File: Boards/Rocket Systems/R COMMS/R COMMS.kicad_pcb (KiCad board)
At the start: 4 copper layers, 75 x 40 mm, 87 parts, among them IC1 NSVT30010MXV6T1G, IC2 NSVT30010MXV6T1G, J1 BM03B-SRSS-TBLFSN, J2 22285061, J3 DX07S016JA1R1500, J4 MEM2061-01-188-00-A_REVA, J5 1190297, J6 SMARA_CONNECTOR, U1 W25Q128JVSIQ TR, U2 ESD7L5.0DT5G, U3 SX1280IMLTRT, U4 NRF21540-QDAA-R, U5 ST1L05APU33R, U6 MAX485CSA+T, U7 VLMKG3400-GS08, U8 STLM20DD9F, U9 VLMKG3400-GS08

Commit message: 3D Symbols Update and R Comms PCB layout (1)
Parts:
- D1: value PMEG2010ER -> RSX301L-30DDTE25; footprint Diode-Schottky_PMEG2010ER:SODFL3517X110N -> Diode-Schottky_RSX301L:DIOM5026X220N
- J2: moved to B.Cu
- moved J4 179.4 mm to (168.4, 80.3), turned to 90 degrees
- moved C1 175.5 mm to (158.0, 80.0)
- moved R30 156.0 mm to (142.9, 59.6), turned to -90 degrees
- moved R31 153.1 mm to (144.8, 64.8), turned to -90 degrees
- moved R29 152.8 mm to (144.8, 59.7)
- moved U6 145.3 mm to (149.9, 62.2), turned to 0 degrees
- moved CV4 141.7 mm to (125.2, 75.6), turned to 0 degrees
- moved R28 138.9 mm to (156.8, 60.4)
- moved R26 135.9 mm to (154.9, 62.2), turned to -90 degrees
- moved CV1 135.2 mm to (125.2, 74.3), turned to 180 degrees
- moved R27 134.9 mm to (156.8, 64.2)
- moved CV6 134.8 mm to (137.7, 77.5), turned to 0 degrees
- moved MCU1 130.7 mm to (131.4, 74.9)
- moved CV8 129.7 mm to (130.2, 68.6)
- moved CV3 128.4 mm to (137.7, 76.2), turned to 0 degrees
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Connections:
- net CRYSTAL renamed /RP2040/Crystal
- J3 pad 11: Net-(D1-PadA) -> Net-(D1-A)
- J3 pad 2: Net-(D1-PadA) -> Net-(D1-A)
- J4 pad 9: /SD-Card SPI MISO -> GND
- J5 pad 1: /RS_B -> /RS_A
- J5 pad 2: /RS_B -> /RS_A
- J5 pad 3: /RS_A -> /RS_B
- J5 pad 4: /RS_A -> /RS_B
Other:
- board size 75 x 40 mm -> 75 x 35 mm

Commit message: R COMMS layout placement
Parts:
- C19, C20, C21, C23, C24, C27, C28, C32, C33, C34, C35, CV12, CV14, CV15, CV16, CV17, CV2, CV3, CV4, D1, IC1, IC2, L2, L3, L4, R12, R14, R15, R16, R26, R27, R28, R29, R30, R31, R8, R9, U3, U4, U5, U6, XTAL2: moved to B.Cu
- R2, R3: footprint Resistor-0603:RES_0603 -> Resistor-0402:RES_0402
- moved R6 178.5 mm to (108.3, 81.5)
- moved R5 176.9 mm to (105.9, 76.4)
- moved XTAL1 176.3 mm to (116.1, 70.7), turned to -90 degrees
- moved R4 175.2 mm to (106.6, 79.0), turned to 0 degrees
- moved R1 170.3 mm to (110.4, 80.9), turned to 0 degrees
- moved J1 167.4 mm to (102.7, 78.0), turned to -90 degrees
- moved R7 167.3 mm to (117.2, 67.3)
- moved CV13 151.4 mm to (118.8, 71.2)
- moved CV5 150.9 mm to (120.8, 83.8), turned to -90 degrees
- moved R13 150.8 mm to (141.3, 78.1), turned to 180 degrees
- moved CV9 148.5 mm to (115.8, 78.0), turned to 180 degrees
- moved CV14 147.7 mm to (127.5, 77.6), turned to 0 degrees
- moved CV7 146.2 mm to (125.6, 72.4), turned to 0 degrees
- moved S3 145.9 mm to (110.0, 85.1)
- moved CV12 144.2 mm to (127.5, 78.9), turned to 0 degrees
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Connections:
- U2 pad 1: /RP2040/USB_DM -> unconnected-(U2-Pad1)
- U2 pad 2: /RP2040/USB_DP -> unconnected-(U2-Pad2)
- U2 pad 3: GND -> unconnected-(U2-Pad3)
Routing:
- net Net-(J1-Pad1): track 0.00 -> 1.91 mm
- net Net-(J1-Pad3): track 0.00 -> 1.81 mm
- net /RS_A: track 0.00 -> 0.50 mm

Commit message: 3D models update
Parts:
- CR2, CR3: footprint LED-Yellow_VLMY1300-GS08:LED_VISHAY_VLMX1300_VIS -> LED-Yellow_VLMY1300-GS08:LEDC1608X100N
- XTAL1: footprint AS12MHz:ASE-3.2X2.5_ABR -> AS12MHz:ASE24576MHZLCT
- moved CV13 7.18 mm to (111.6, 71.9), turned to -90 degrees
- moved R7 2.22 mm to (115.0, 67.6), turned to 0 degrees
- moved R26 1.36 mm to (151.4, 65.3)
- moved R27 1.36 mm to (152.7, 63.9)
- moved R29 1.36 mm to (142.4, 67.8)
- moved R31 1.36 mm to (142.4, 62.5)
- moved U6 1.36 mm to (146.9, 65.3)
- moved R30 1.36 mm to (141.1, 62.5)
- moved R28 1.25 mm to (152.7, 66.8)
- moved XTAL1 1.07 mm to (115.0, 70.9)
- moved L1 0.60 mm to (109.0, 69.3), turned to 90 degrees
- moved J5 0.28 mm to (156.5, 67.8)
- moved L4 0.20 mm to (100.8, 81.3)
- moved CR2 0.13 mm to (151.2, 76.6)
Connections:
- J5 pad 1: /RS_A -> /RS_B
- J5 pad 2: /RS_A -> /RS_B
- J5 pad 3: /RS_B -> /RS_A
- J5 pad 4: /RS_B -> /RS_A
- U2 pad 1: unconnected-(U2-Pad1) -> /RP2040/USB_DP
- U2 pad 2: unconnected-(U2-Pad2) -> /RP2040/USB_DM
- U2 pad 3: unconnected-(U2-Pad3) -> GND
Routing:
- net /RS_A: track 0.50 -> 0.00 mm

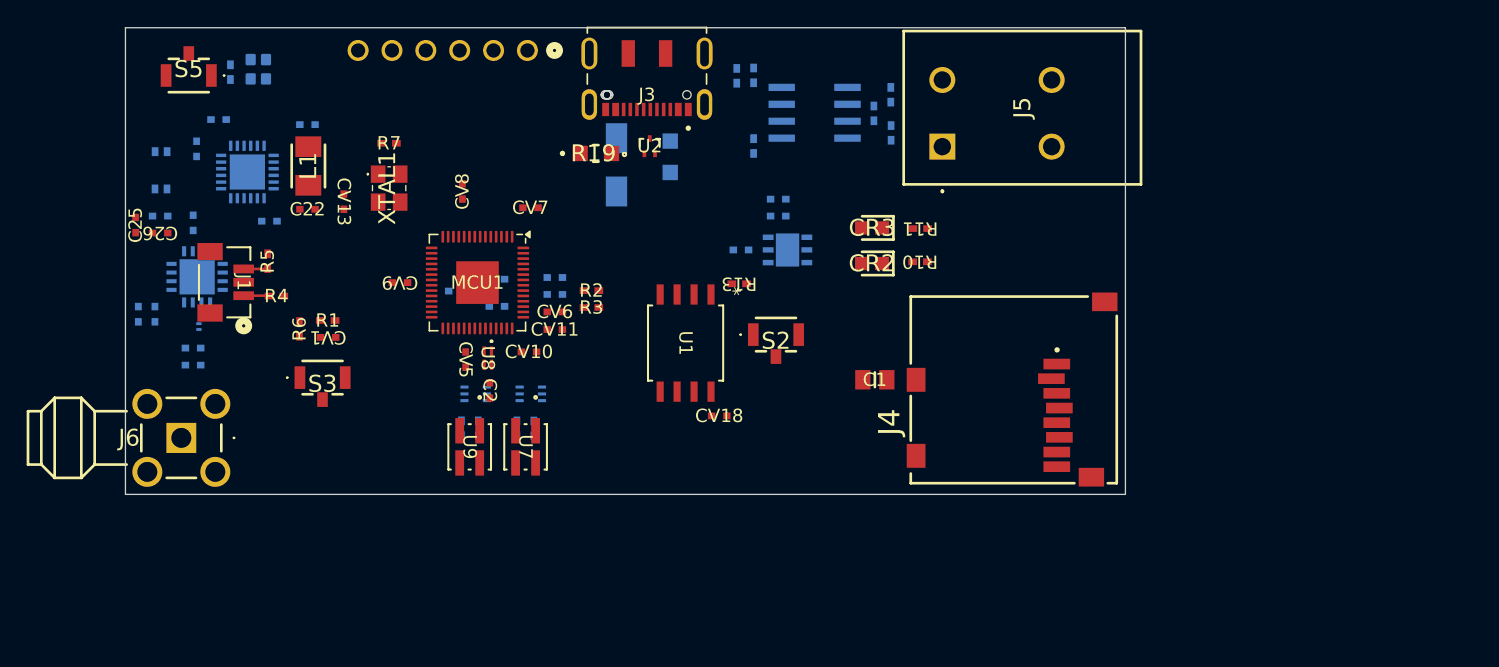
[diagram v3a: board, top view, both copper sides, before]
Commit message: R COMMS layout placement update
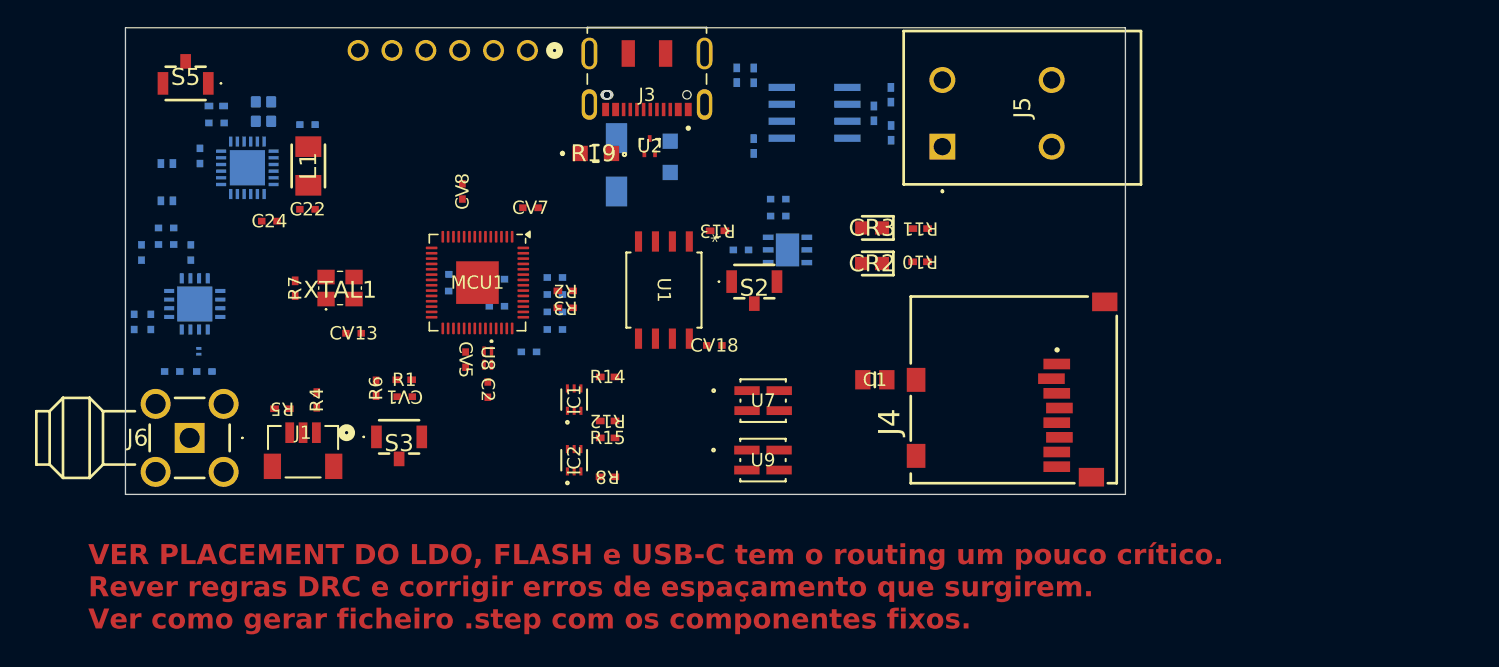
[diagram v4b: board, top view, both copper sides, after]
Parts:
- C24, IC1, IC2, R12, R14, R15, R8: moved to F.Cu
- C25, C26, CV10, CV11, CV6, CV9: moved to B.Cu
- moved U9 22.0 mm to (143.1, 91.3), turned to 0 degrees
- moved U7 18.2 mm to (143.1, 86.9), turned to 0 degrees
- moved J1 14.0 mm to (108.6, 90.7), turned to 0 degrees
- moved R7 12.9 mm to (108.0, 78.4), turned to 90 degrees
- moved R8 11.5 mm to (131.4, 92.6), turned to 180 degrees
- moved R5 11.1 mm to (107.0, 87.5), turned to 180 degrees
- moved CV13 9.90 mm to (112.4, 81.8), turned to 0 degrees
- moved R15 9.72 mm to (131.4, 89.7), turned to 0 degrees
- moved IC2 8.91 mm to (128.9, 91.3), turned to 90 degrees
- moved R4 8.36 mm to (109.6, 86.8), turned to 90 degrees
- moved XTAL1 8.35 mm to (111.3, 78.4), turned to 0 degrees
- moved R6 7.26 mm to (114.0, 85.9)
- moved S3 7.26 mm to (115.8, 89.6)
- moved CV1 7.26 mm to (116.2, 86.6)
- moved R1 7.26 mm to (116.2, 85.3)
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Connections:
- C2 pad 2: Net-(U8-GND) -> GND
- U8 pad 3: Net-(U8-GND) -> GND
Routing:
- net Net-(J1-Pad1): track 1.91 -> 0.00 mm
- net Net-(J1-Pad3): track 1.81 -> 0.00 mm
- added copper zone on In2.Cu, net GND
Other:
- board text added: "VER PLACEMENT DO LDO, FLASH e USB-C tem o routing um pouco crítico. Rever regras DRC e corrigir erros de espaçamento que surgirem. Ver como gerar ficheiro .step com os componentes fixos."

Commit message: full update on RCOMMS layout
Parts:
- removed R12, R14: 100, Resistor-0402:RES_0402
- removed R31: 10K, Resistor-0402:RES_0402
- removed S2, S3, S5: TL1017AABF160QG, E-Switch_Small:TL1017AABF160QG
- added C29: 4.7u, Capacitor-0402:Capacitor_0402, F.Cu at (129.9, 63.4)
- added C30: 100nF, Capacitor-0402:Capacitor_0402, F.Cu at (162.8, 81.9)
- added C31: 100nF, Capacitor-0402:Capacitor_0402, F.Cu at (160.8, 73.7)
- added C36: 100n, Capacitor-0402:Capacitor_0402, F.Cu at (156.5, 72.1)
- added C37: 100nF, Capacitor-0402:Capacitor_0402, F.Cu at (161.6, 81.9)
- added C38: 100nF, Capacitor-0402:Capacitor_0402, F.Cu at (160.8, 75.0)
- added C39: 100nF, Capacitor-0402:Capacitor_0402, F.Cu at (175.8, 65.2)
- added C40: 4.7u, Capacitor-0402:Capacitor_0402, F.Cu at (129.9, 64.6)
- added C41: 100nF, Capacitor-0402:Capacitor_0402, F.Cu at (119.3, 64.8)
- added H1: MountingHole, MountingHole:MountingHole_3.2mm_M3_ISO7380_Pad_TopBottom, F.Cu at (110.0, 63.0)
- added H2: MountingHole, MountingHole:MountingHole_3.2mm_M3_ISO7380_Pad_TopBottom, F.Cu at (170.0, 63.0)
- added H3: MountingHole, MountingHole:MountingHole_3.2mm_M3_ISO7380_Pad_TopBottom, F.Cu at (110.0, 92.0)
- added H4: MountingHole, MountingHole:MountingHole_3.2mm_M3_ISO7380_Pad_TopBottom, F.Cu at (170.0, 92.0)
- added IC3: THVD2412VDR, THVD2412VDR:SOIC127P600X175-14N, F.Cu at (166.8, 76.8)
- added JP1: Jumper_2_Bridged, Jumper:SolderJumper-2_P1.3mm_Open_RoundedPad1.0x1.5mm, B.Cu at (109.2, 82.0)
- added JP2: Jumper_2_Bridged, Jumper:SolderJumper-2_P1.3mm_Open_RoundedPad1.0x1.5mm, B.Cu at (142.2, 92.0)
- added JP3: Jumper_2_Bridged, Jumper:SolderJumper-2_P1.3mm_Open_RoundedPad1.0x1.5mm, B.Cu at (134.4, 67.1)
- added LS1: PKLCS1212E20A0-R1, PKLCS1212E20A0-R1:PKLCS1212E20A0-R1, B.Cu at (151.9, 80.5)
- added MP1: S0991-46R, S0991-46R:S099146R, F.Cu at (93.0, 76.3)
- added MP2: S0991-46R, S0991-46R:S099146R, F.Cu at (118.0, 76.5)
- added MP3: S0991-46R, S0991-46R:S099146R, F.Cu at (103.0, 66.5)
- added MP4: S0991-46R, S0991-46R:S099146R, F.Cu at (111.0, 86.5)
- added R17: 1k, Resistor-0402:RES_0402, F.Cu at (153.1, 76.4)
- added R18: 1k, Resistor-0402:RES_0402, F.Cu at (152.7, 82.3)
- added R21: 10k, Resistor-0402:RES_0402, F.Cu at (164.2, 81.9)
- added R22: 10k, Resistor-0402:RES_0402, F.Cu at (172.7, 74.9)
- added R23: 10k, Resistor-0402:RES_0402, F.Cu at (172.7, 73.7)
- added R24: 120, Resistor-0402:RES_0402, F.Cu at (166.1, 72.3)
- added R25: 120, Resistor-0402:RES_0402, F.Cu at (168.7, 72.3)
- C19, C20, C21, C23, C25, C26, C27, C28, C32, C33, C34, C35, CV10, CV11, CV12, CV14, CV15, CV16, CV17, CV2, CV3, CV4, CV6, CV9, D1, L2, L3, L4, R16, U3, U4, U5, XTAL2: moved to F.Cu
- IC1: value NSVT30010MXV6T1G -> BC846BLT1G; footprint 2 PNP:SOT-563_1P3X1P7_ONS -> BJT NPN:SOT96P237X111-3N
- J5: value 1190297 -> 5023520600; footprint LPT Conn 2 Entradas:1190297 -> 5023520600:CONN06_502352_MOL
- MCU1: footprint Package_DFN_QFN:QFN-56-1EP_7x7mm_P0.4mm_EP3.2x3.2mm -> RP2040:QFN56_7X7_RPI
- R19: footprint Resistor-0805:RES_0805 -> Resistor-0402:RES_0402
- R26: value 120 -> 523; moved to F.Cu
- R27, R28: value 20K -> 523; moved to F.Cu
- R29: value 10K -> 523; moved to F.Cu
- R30: value 10K -> 10k; moved to F.Cu
- R9: footprint Resistor-0805:RES_0805 -> Resistor-0402:RES_0402; moved to F.Cu
- U2: value ESD7L5.0DT5G -> IP4220CZ6; footprint ESD7L5-Diode:SOT-723_0P85X1P25_ONS -> IP4220CZ6:SOT457_NEX
- U6: value MAX485CSA+T -> IP4220CZ6; footprint RS Transceiver:21-0041-3-M_90-0096-8L_MXM -> IP4220CZ6:SOT457_NEX; moved to F.Cu
- U7: value VLMKG3400-GS08 -> IP4220CZ6; footprint VLMKG3400-GS08:SMT_00-GS08_VIS -> IP4220CZ6:SOT457_NEX
- moved R30 32.2 mm to (166.7, 81.9), turned to 90 degrees
- moved R29 31.8 mm to (172.7, 77.3), turned to 0 degrees
- moved U7 30.1 mm to (122.7, 64.8), turned to 180 degrees
- moved U6 29.1 mm to (175.8, 68.6), turned to 90 degrees
- moved J5 28.1 mm to (184.5, 70.6)
- moved R8 28.0 mm to (159.1, 88.1), turned to -90 degrees
- moved IC2 27.7 mm to (156.6, 90.5), turned to 180 degrees
- moved J1 27.5 mm to (136.1, 91.9)
- moved R5 27.5 mm to (134.5, 88.7)
- moved R6 26.7 mm to (140.4, 90.6)
- moved R1 26.5 mm to (142.3, 90.0), turned to 180 degrees
- moved CV1 26.5 mm to (142.3, 91.3), turned to 0 degrees
- moved IC1 25.0 mm to (152.7, 79.0), turned to -90 degrees
- moved R15 22.8 mm to (154.2, 88.1), turned to 90 degrees
- moved R4 22.5 mm to (131.8, 90.6)
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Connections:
- net Net-(MCU1-USB_DM) renamed /RP2040/USB_D-
- net Net-(MCU1-USB_DP) renamed /RP2040/USB_D+
- D1 pad 2: Net-(D1-A) -> VBUS
- IC1 pad 2: /Status2 Green -> GND
- IC1 pad 3: GND -> Net-(IC1-C)
- J2 pad 2: /OBC UART TX -> GND
- J2 pad 3: /OBC UART RX -> /OBC UART TX
- J2 pad 4: /OBC UART CTS -> /OBC UART RX
- J2 pad 5: /OBC UART RTS -> /OBC UART CTS
- J2 pad 6: GND -> /OBC UART RTS
- J3 pad 11: Net-(D1-A) -> VBUS
- J3 pad 2: Net-(D1-A) -> VBUS
- J3 pad 5: /RP2040/USB_DM -> /RP2040/USB_DN
- J3 pad 8: /RP2040/USB_DM -> /RP2040/USB_DN
- J5 pad 1: /RS_B -> /Pyro Main Chute
- J5 pad 2: /RS_B -> /Pyro Drogue
- J5 pad 3: /RS_A -> /RS-TX_DP
- J5 pad 4: /RS_A -> /RS-TX_DN
- MCU1 pad 40: /Status2 Green -> /Pyro Main Chute
- MCU1 pad 41: /Status2 Red -> /Pyro Drogue
- MCU1 pad 6: /RS_RX -> /RS_TX
- MCU1 pad 7: /RS_TX -> /RS_RX
- MCU1 pad 8: /RS_ENABLE -> /Buzzer
- R19 pad 1: GND -> Net-(J3-CC2)
- R19 pad 2: Net-(J3-CC2) -> GND
- R26 pad 1: /RS_B -> /RS-RX_DN
- R26 pad 2: /RS_A -> GND
- R27 pad 2: /RS_A -> /RS-RX_DP
- R28 pad 1: /RS_B -> +5V
- R28 pad 2: GND -> /RS-TX_DP
- R29 pad 1: +3.3V -> /RS-TX_DN
- R29 pad 2: /RS_RX -> GND
- R3 pad 1: /RP2040/USB_DM -> /RP2040/USB_DN
- R30 pad 2: /RS_ENABLE -> Net-(IC3-DE)
- U2 pad 2: /RP2040/USB_DM -> GND
- U2 pad 3: GND -> /RP2040/USB_DN
- U6 pad 1: /RS_RX -> /RS-TX_DN
- U6 pad 2: /RS_ENABLE -> GND
- U6 pad 3: /RS_ENABLE -> /RS-TX_DP
- U6 pad 4: /RS_TX -> /RS-RX_DN
- U6 pad 5: GND -> +5V
- U6 pad 6: /RS_A -> /RS-RX_DP
- U7 pad 1: +5V -> /OBC UART TX
- U7 pad 2: Net-(U7-A_Green) -> GND
- U7 pad 3: +5V -> /OBC UART RX
- U7 pad 4: Net-(U7-A_Red) -> /OBC UART RTS
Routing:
- net /OBC UART CTS: track 0.00 -> 19.9 mm
- net /OBC UART TX: track 0.00 -> 18.8 mm
- net /RP2040/USB_DN: track 0.00 -> 18.2 mm
- net Net-(MCU1-RUN): track 0.00 -> 16.6 mm
- net /RP2040/USB_DP: track 0.00 -> 15.0 mm
- net /OBC UART RX: track 0.00 -> 14.6 mm
- net Net-(MCU1-SWCLK): track 0.00 -> 8.11 mm
- net /RP2040/USB_D+: track 0.00 -> 7.75 mm
- net VBUS: track 0.00 -> 7.59 mm, vias 0 -> 1
- net /RP2040/USB_D-: track 0.00 -> 7.39 mm
- net Net-(MCU1-SWD): track 0.00 -> 7.24 mm
- net +5V: track 0.00 -> 6.92 mm
- net Net-(J1-Pad1): track 0.00 -> 6.35 mm
- net +3.3V: track 0.00 -> 5.82 mm
- net /RP2040/Crystal: track 0.00 -> 5.77 mm
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- removed copper zone on In2.Cu, net GND
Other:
- board size 75 x 35 mm -> 100 x 35 mm
- board text added: "RFI Shield Can"
- board text removed: "VER PLACEMENT DO LDO, FLASH e USB-C tem o routing um pouco crítico. Rever regras DRC e corrigir erros de espaçamento que surgirem. Ver como gerar ficheiro .step com os componentes fixos."

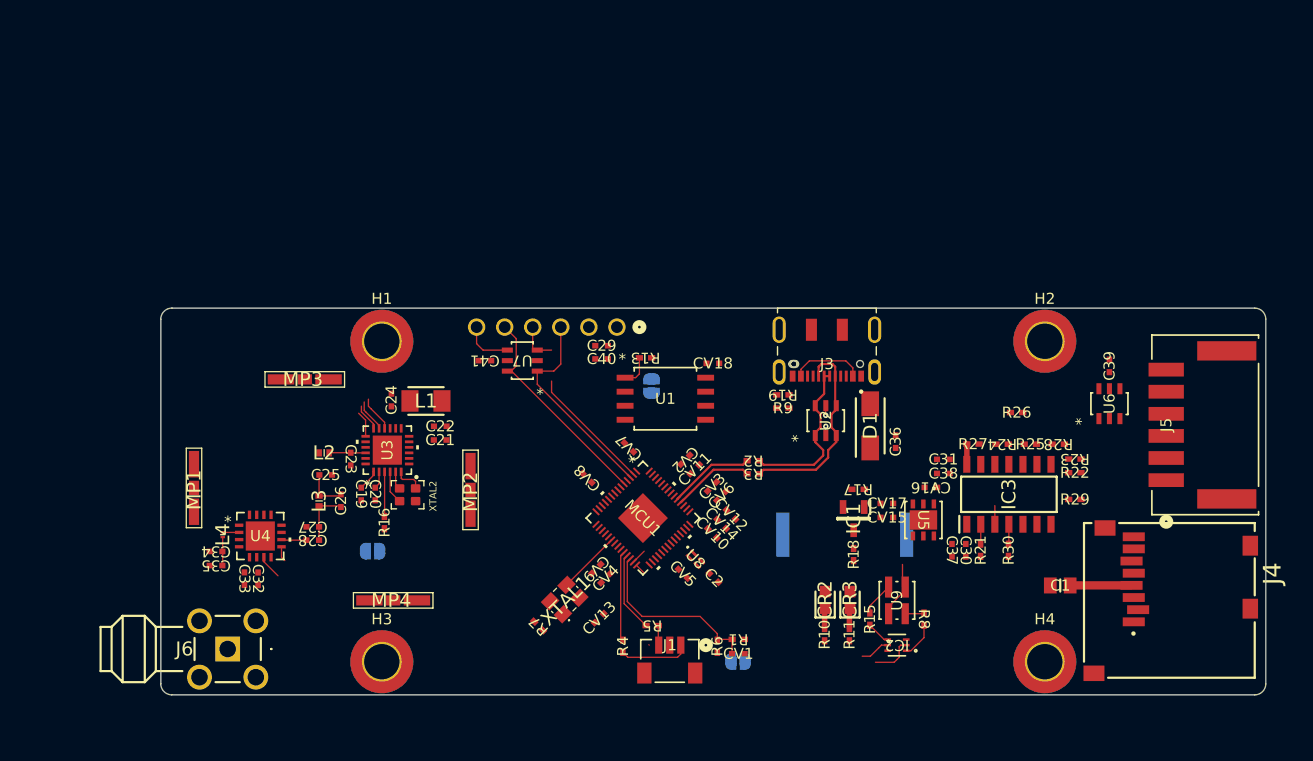
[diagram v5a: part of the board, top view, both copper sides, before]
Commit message: TVCS refactor
Muitas alterações e correções na placa TVCSO:
Novo ADC, filtros passa baixo, novo RS transceiver, reformulação de
conexões
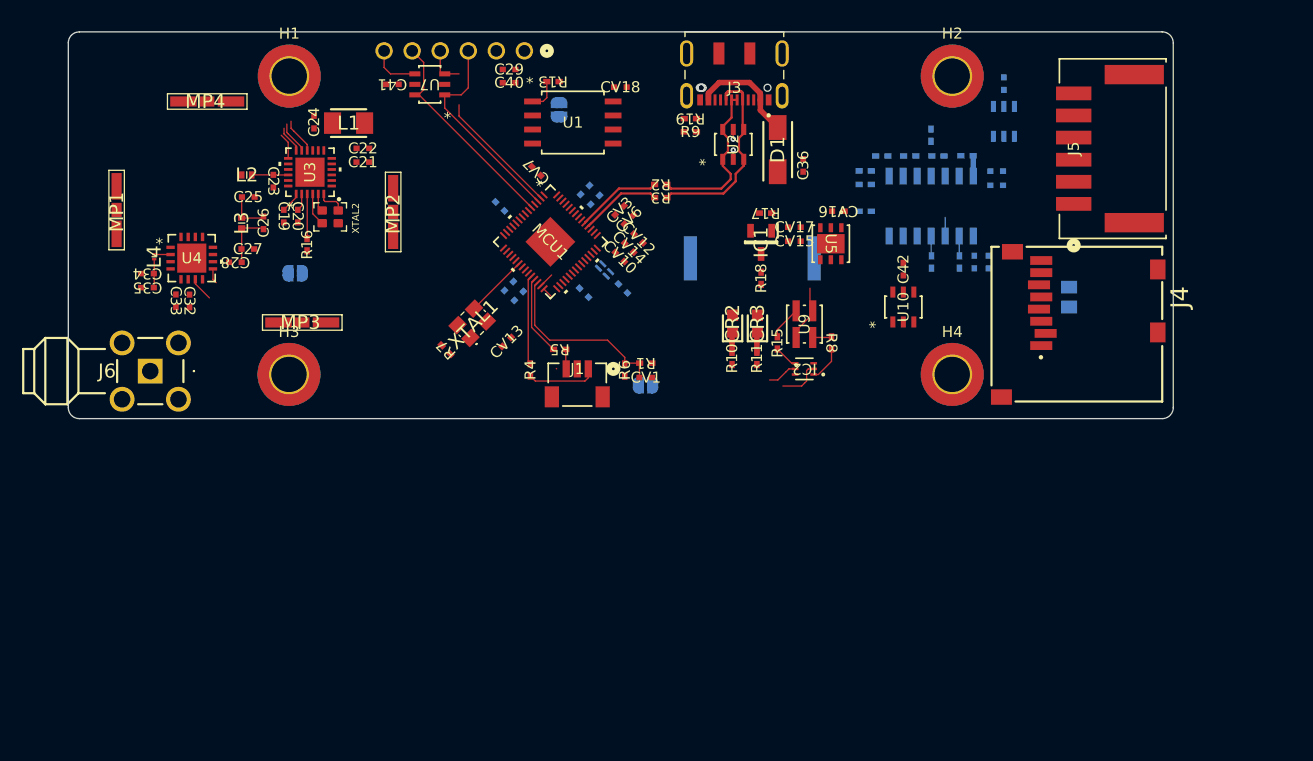
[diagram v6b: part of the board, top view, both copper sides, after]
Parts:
- added C42: 100nF, Capacitor-0402:Capacitor_0402, F.Cu at (157.2, 56.5)
- added U10: IP4220CZ6, IP4220CZ6:SOT457_NEX, F.Cu at (157.2, 59.9)
- C1, C2, C30, C31, C37, C38, C39, CV11, CV2, CV4, CV5, CV8, CV9, IC3, R21, R22, R23, R24, R25, R26, R27, R28, R29, R30, U6, U8: moved to B.Cu
- moved MP4 48.2 mm to (94.2, 41.3)
- moved R23 32.3 mm to (153.7, 47.6), turned to 0 degrees
- moved R29 32.3 mm to (153.7, 51.2), turned to 180 degrees
- moved R22 32.3 mm to (153.7, 48.8), turned to 180 degrees
- moved R28 30.6 mm to (155.2, 46.2), turned to 0 degrees
- moved R25 28.3 mm to (157.8, 46.2), turned to 180 degrees
- moved U8 27.4 mm to (130.2, 56.5)
- moved C2 27.4 mm to (131.8, 58.2)
- moved H3 27.3 mm to (101.6, 66.0)
- moved H4 27.3 mm to (161.6, 66.0)
- moved U6 27.3 mm to (166.3, 43.1)
- moved C39 27.3 mm to (166.3, 39.7)
- moved IC3 27.0 mm to (159.7, 50.8)
- moved R30 27.0 mm to (159.7, 55.8)
- moved CV5 27.0 mm to (128.3, 58.6)
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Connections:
- MCU1 pad 38: /Temp_Sense -> /Status1 Red
- MCU1 pad 39: /Status1 Red -> /Temp_Sense
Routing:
- net +3.3V: track 5.82 -> 0.26 mm
- net VBUS: track 7.59 -> 10.8 mm
- net Net-(U4-TRX): track 2.28 -> 0.07 mm
- net /RP2040/USB_DN: track 18.2 -> 17.7 mm
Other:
- board text added: "Fazer sinal de corrente para o Pyro Channel Rever placement de alguns condensadores -> Passar para B.Cu Stack up Criar Nets Power and Ground Planes - pesquisar como fazer grounds para RF Ver questão de Vias on pad Guard Rings e como fazer routing com eles Fazer routing 1- RF 2- Differential pairs + length tunning 3- Digital 4- Analógico Via Stitching Silk Screen Solder Mask"
